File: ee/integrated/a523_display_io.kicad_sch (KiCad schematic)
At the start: 5 parts, among them U201 A523

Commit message: Working on the schematic.
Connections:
- net DSI_CKN renamed DSI.CKN
- net DSI_CKP renamed DSI.CKP
- net DSI_D0N renamed DSI.D0N
- net DSI_D0P renamed DSI.D0P
- net DSI_D1N renamed DSI.D1N
- net DSI_D1P renamed DSI.D1P
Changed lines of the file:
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@@
 		(at 114.3 71.12)
 	)
+	(bus_entry
+		(at 30.48 48.26)
+		(size 2.54 2.54)
+		(stroke
+			(width 0)
+			(type default)
+		)
+	)
+	(bus_entry
+		(at 30.48 45.72)
+		(size 2.54 2.54)
+		(stroke
+			(width 0)
+			(type default)
+		)
+	)
+	(bus_entry
+		(at 30.48 35.56)
+		(size 2.54 2.54)
+		(stroke
+			(width 0)
+			(type default)
+		)
+	)
+	(bus_entry
+		(at 30.48 43.18)
+		(size 2.54 2.54)
+		(stroke
+			(width 0)
+			(type default)
+		)
+	)
+	(bus_entry
+		(at 30.48 38.1)
+		(size 2.54 2.54)
+		(stroke
+			(width 0)
+			(type default)
+		)
+	)
+	(bus_entry
+		(at 30.48 40.64)
+		(size 2.54 2.54)
+		(stroke
+			(width 0)
+			(type default)
+		)
+	)
+	(bus
+		(pts
+			(xy 24.13 29.21) (xy 30.48 29.21)
+		)
+		(stroke
+			(width 0)
+			(type default)
+		)
+	)
 	(wire
 		(pts
@@
 	(wire
 		(pts
-			(xy 53.34 101.6) (xy 48.26 101.6)
+			(xy 43.18 99.06) (xy 43.18 101.6)
 		)
 		(stroke
@@
 	(wire
 		(pts
-			(xy 53.34 43.18) (xy 48.26 43.18)
+			(xy 43.18 101.6) (xy 53.34 101.6)
 		)
 		(stroke
@@
 	(wire
 		(pts
-			(xy 53.34 50.8) (xy 48.26 50.8)
+			(xy 172.72 40.64) (xy 187.96 40.64)
 		)
 		(stroke
@@
 	(wire
 		(pts
-			(xy 53.34 45.72) (xy 48.26 45.72)
+			(xy 48.26 95.25) (xy 48.26 99.06)
 		)
 		(stroke
@@
 	(wire
 		(pts
-			(xy 172.72 40.64) (xy 187.96 40.64)
+			(xy 172.72 48.26) (xy 172.72 50.8)
 		)
 		(stroke
@@
 	(wire
 		(pts
-			(xy 172.72 48.26) (xy 172.72 50.8)
+			(xy 172.72 43.18) (xy 172.72 40.64)
+		)
+		(stroke
+			(width 0)
+			(type default)
+		)
+	)
+	(bus
+		(pts
+			(xy 30.48 29.21) (xy 30.48 48.26)
 		)
 		(stroke
@@
 	(wire
 		(pts
-			(xy 172.72 43.18) (xy 172.72 40.64)
+			(xy 172.72 50.8) (xy 187.96 50.8)
 		)
 		(stroke
@@
 	(wire
 		(pts
-			(xy 172.72 50.8) (xy 187.96 50.8)
+			(xy 53.34 99.06) (xy 48.26 99.06)
 		)
 		(stroke
@@
 	(wire
 		(pts
-			(xy 53.34 99.06) (xy 48.26 99.06)
+			(xy 33.02 43.18) (xy 53.34 43.18)
 		)
 		(stroke
@@
 	(wire
 		(pts
-			(xy 53.34 48.26) (xy 48.26 48.26)
+			(xy 33.02 40.64) (xy 53.34 40.64)
 		)
 		(stroke
@@
 	(wire
 		(pts
-			(xy 53.34 40.64) (xy 48.26 40.64)
+			(xy 33.02 50.8) (xy 53.34 50.8)
 		)
 		(stroke
@@
 	(wire
 		(pts
-			(xy 53.34 38.1) (xy 48.26 38.1)
+			(xy 33.02 45.72) (xy 53.34 45.72)
 		)
 		(stroke
@@
 	(wire
 		(pts
+			(xy 33.02 38.1) (xy 53.34 38.1)
+		)
+		(stroke
+			(width 0)
+			(type default)
+		)
+	)
+	(wire
+		(pts
 			(xy 114.3 78.74) (xy 119.38 78.74)
 		)
@@
 		)
 	)
-	(hierarchical_label "DSI_CKN"
-		(shape bidirectional)
-		(at 48.26 50.8 180)
+	(wire
+		(pts
+			(xy 33.02 48.26) (xy 53.34 48.26)
+		)
+		(stroke
+			(width 0)
+			(type default)
+		)
+	)
+	(label "DSI.D0N"
+		(at 52.07 40.64 180)
 		(effects
 			(font
 				(size 1.27 1.27)
 			)
-			(justify right)
-		)
-	)
-	(hierarchical_label "DSI_CKP"
-		(shape bidirectional)
-		(at 48.26 48.26 180)
+			(justify right bottom)
+		)
+	)
+	(label "DSI.CKN"
+		(at 52.07 50.8 180)
 		(effects
 			(font
 				(size 1.27 1.27)
 			)
-			(justify right)
-		)
-	)
-	(hierarchical_label "DSI_D1P"
-		(shape bidirectional)
-		(at 48.26 43.18 180)
+			(justify right bottom)
+		)
+	)
+	(label "DSI.CKP"
+		(at 52.07 48.26 180)
 		(effects
 			(font
 				(size 1.27 1.27)
 			)
-			(justify right)
-		)
-	)
-	(hierarchical_label "DSI_D1N"
-		(shape bidirectional)
-		(at 48.26 45.72 180)
+			(justify right bottom)
+		)
+	)
+	(label "DSI.D1N"
+		(at 52.07 45.72 180)
 		(effects
 			(font
 				(size 1.27 1.27)
 			)
-			(justify right)
-		)
-	)
-	(hierarchical_label "DSI_D0P"
-		(shape bidirectional)
-		(at 48.26 38.1 180)
+			(justify right bottom)
+		)
+	)
+	(label "DSI.D1P"
+		(at 52.07 43.18 180)
 		(effects
 			(font
 				(size 1.27 1.27)
 			)
-			(justify right)
-		)
-	)
-	(hierarchical_label "DSI_D0N"
-		(shape bidirectional)
-		(at 48.26 40.64 180)
+			(justify right bottom)
+		)
+	)
+	(label "DSI.D0P"
+		(at 52.07 38.1 180)
 		(effects
 			(font
 				(size 1.27 1.27)
 			)
+			(justify right bottom)
+		)
+	)
+	(hierarchical_label "DSI{DSI}"
+		(shape bidirectional)
+		(at 24.13 29.21 180)
+		(effects
+			(font
+				(size 1.27 1.27)
+			)
 			(justify right)
 		)
@@
 	(symbol
 		(lib_id "A523Power:VCC_3V3")
-		(at 48.26 99.06 90)
+		(at 48.26 95.25 0)
 		(unit 1)
 		(body_style 1)
@@
 		(dnp no)
 		(property "Reference" "#PWR0180313568"
-			(at 48.26 99.06 0)
+			(at 48.26 95.25 0)
 			(hide yes)
 			(show_name no)
@@
 		)
 		(property "Value" "VCC_3V3"
-			(at 41.015 99.06 90)
+			(at 48.514 91.694 0)
 			(show_name no)
 			(do_not_autoplace no)
@@
 		)
 		(property "Footprint" ""
-			(at 48.26 99.06 0)
+			(at 48.26 95.25 0)
 			(show_name no)
 			(do_not_autoplace no)
@@
 		)
 		(property "Datasheet" ""
-			(at 48.26 99.06 0)
+			(at 48.26 95.25 0)
 			(show_name no)
 			(do_not_autoplace no)
@@
 		)
 		(property "Description" ""
-			(at 48.26 99.06 0)
+			(at 48.26 95.25 0)
 			(show_name no)
 			(do_not_autoplace no)
@@
 	(symbol
 		(lib_id "A523Power:VCC_1V8")
-		(at 48.26 101.6 90)
+		(at 43.18 99.06 0)
 		(unit 1)
 		(body_style 1)
@@
 		(dnp no)
 		(property "Reference" "#PWR0853362114"
-			(at 48.26 101.6 0)
+			(at 43.18 99.06 0)
 			(hide yes)
 			(show_name no)
@@
 		)
 		(property "Value" "VCC_1V8"
-			(at 41.015 101.6 90)
+			(at 43.18 95.25 0)
 			(show_name no)
 			(do_not_autoplace no)
@@
 		)
 		(property "Footprint" ""
-			(at 48.26 101.6 0)
+			(at 43.18 99.06 0)
 			(show_name no)
 			(do_not_autoplace no)
@@
 		)
 		(property "Datasheet" ""
-			(at 48.26 101.6 0)
+			(at 43.18 99.06 0)
 			(show_name no)
 			(do_not_autoplace no)
@@
 		)
 		(property "Description" ""
-			(at 48.26 101.6 0)
-			(show_name no)
-			(do_not_autoplace no)
+			(at 43.18 99.06 0)
+			(show_name no)
+			(do_not_autoplace no)

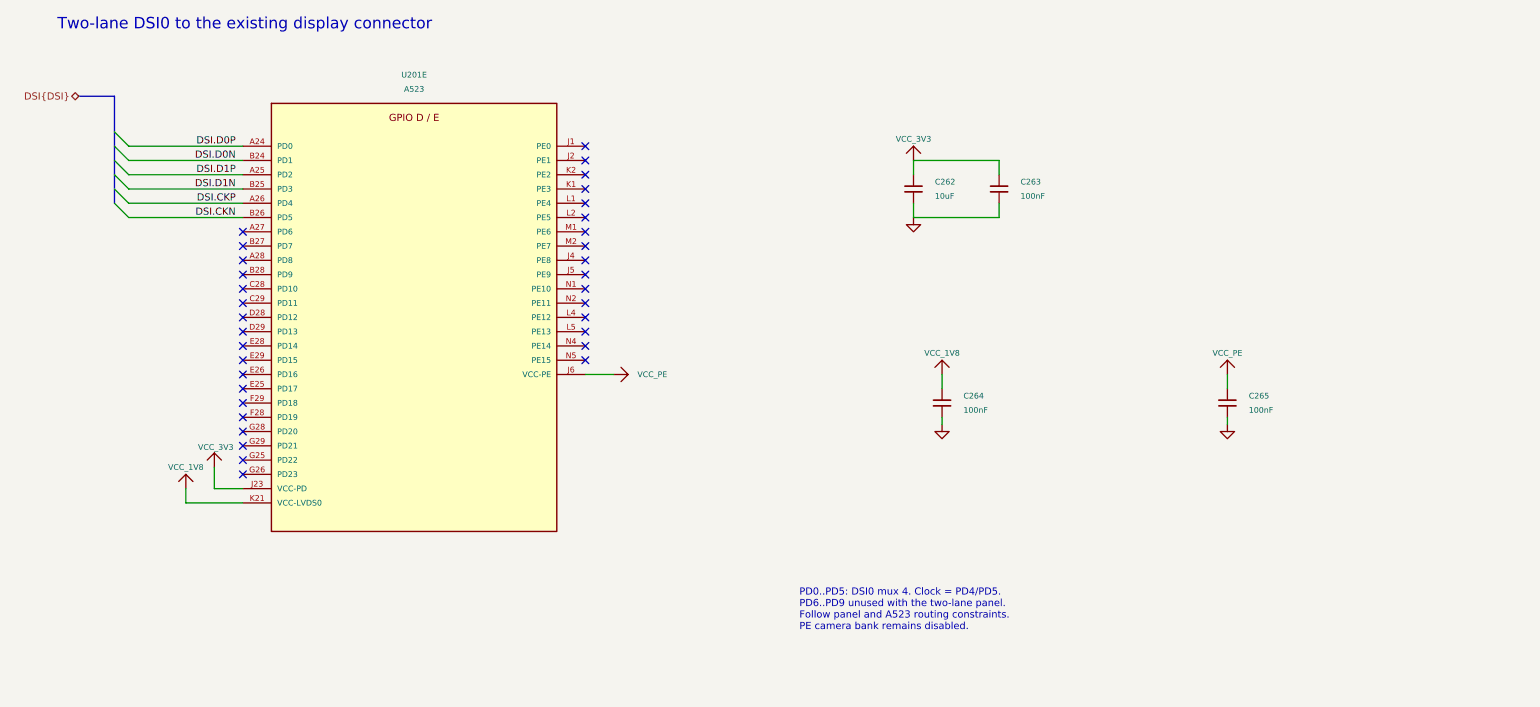
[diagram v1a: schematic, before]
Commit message: Removed USB sheets and moved the parts to the main sheets.
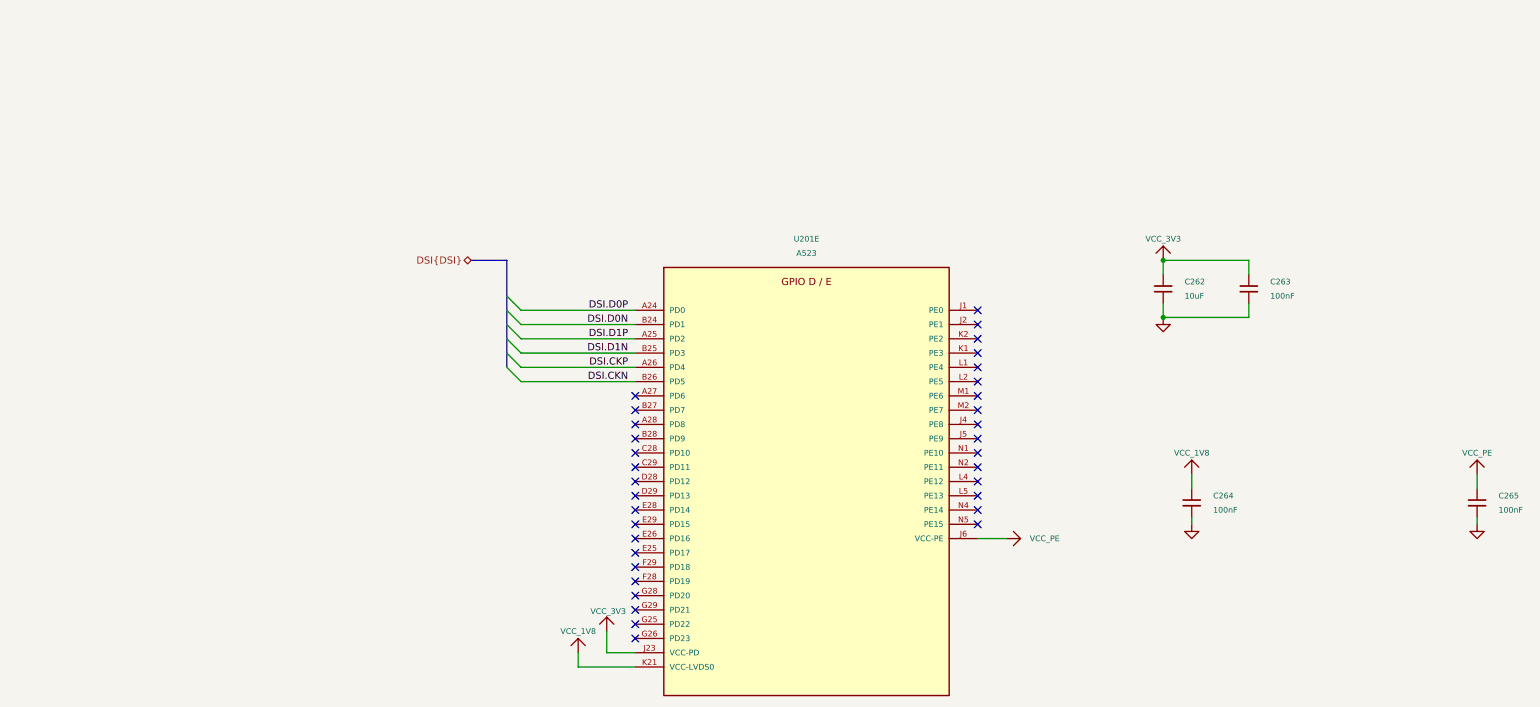
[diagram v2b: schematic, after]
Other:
- note removed: "PD0..PD5: DSI0 mux 4. Clock = PD4/PD5. PD6..PD9 unused with the two-lane panel. Follow panel and A523 routing constraints. PE camera bank remains disabled."
- note removed: "Two-lane DSI0 to the existing display connector"
- moved on the sheet: C262, C263, C264, C265, U201E

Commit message: Worked on the layout.
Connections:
- net VCC_PE renamed +3V3
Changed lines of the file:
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@@
+	(wire
+		(pts
+			(xy 187.96 104.14) (xy 187.96 107.95)
+		)
+		(stroke
+			(width 0)
+			(type default)
+		)
+	)
 	(wire
 		(pts
@@
 	(wire
 		(pts
-			(xy 184.15 107.95) (xy 189.23 107.95)
+			(xy 184.15 107.95) (xy 187.96 107.95)
 		)
 		(stroke
@@
 	)
 	(symbol
+		(lib_id "power:+5V")
+		(at 273.05 96.52 0)
+		(unit 1)
+		(body_style 1)
+		(exclude_from_sim no)
+		(in_bom yes)
+		(on_board yes)
+		(in_pos_files yes)
+		(dnp no)
+		(fields_autoplaced yes)
+		(property "Reference" "#PWR023"
+			(at 273.05 100.33 0)
+			(hide yes)
+			(show_name no)
+			(do_not_autoplace no)
+			(effects
+				(font
+					(size 1.27 1.27)
+				)
+			)
+		)
+		(property "Value" "+3V3"
+			(at 273.05 93.0181 0)
+			(show_name no)
+			(do_not_autoplace no)
+			(effects
+				(font
+					(size 1.27 1.27)
+				)
+			)
+		)
+		(property "Footprint" ""
+			(at 273.05 96.52 0)
+			(hide yes)
+			(show_name no)
+			(do_not_autoplace no)
+			(effects
+				(font
+					(size 1.27 1.27)
+				)
+			)
+		)
+		(property "Datasheet" ""
+			(at 273.05 96.52 0)
+			(hide yes)
+			(show_name no)
+			(do_not_autoplace no)
+			(effects
+				(font
+					(size 1.27 1.27)
+				)
+			)
+		)
+		(property "Description" ""
+			(at 273.05 96.52 0)
+			(show_name no)
+			(do_not_autoplace no)
+			(effects
+				(font
+					(size 1.27 1.27)
+				)
+			)
+		)
+		(pin "1"
+		)
+		(instances
+			(project "blackpants"
+				(path "/d0a98fce-b133-4503-8f8a-83b2a1eed591/9a57dc4c-c52c-4694-b419-f0eeecdbb748"
+					(reference "#PWR023")
+					(unit 1)
+				)
+			)
+		)
+	)
+	(symbol
 		(lib_id "power:GND")
 		(at 273.05 105.41 0)
@@
 				(path "/d0a98fce-b133-4503-8f8a-83b2a1eed591/9a57dc4c-c52c-4694-b419-f0eeecdbb748"
 					(reference "#PWR0250221326")
-					(unit 1)
-				)
-			)
-		)
-	)
-	(symbol
-		(lib_id "A523Power:VCC_PE")
-		(at 189.23 107.95 270)
-		(unit 1)
-		(body_style 1)
-		(exclude_from_sim no)
-		(in_bom no)
-		(on_board yes)
-		(in_pos_files yes)
-		(dnp no)
-		(property "Reference" "#PWR0203783563"
-			(at 189.23 107.95 0)
-			(hide yes)
-			(show_name no)
-			(do_not_autoplace no)
-			(effects
-				(font
-					(size 1.016 1.016)
-				)
-			)
-		)
-		(property "Value" "VCC_PE"
-			(at 196.075 107.95 270)
-			(show_name no)
-			(do_not_autoplace no)
-			(effects
-				(font
-					(size 1.016 1.016)
-				)
-			)
-		)
-		(property "Footprint" ""
-			(at 189.23 107.95 0)
-			(show_name no)
-			(do_not_autoplace no)
-			(effects
-				(font
-					(size 1.27 1.27)
-				)
-			)
-		)
-		(property "Datasheet" ""
-			(at 189.23 107.95 0)
-			(show_name no)
-			(do_not_autoplace no)
-			(effects
-				(font
-					(size 1.27 1.27)
-				)
-			)
-		)
-		(property "Description" ""
-			(at 189.23 107.95 0)
-			(show_name no)
-			(do_not_autoplace no)
-			(effects
-				(font
-					(size 1.27 1.27)
-				)
-			)
-		)
-		(pin "1"
-		)
-		(instances
-			(project "blackpants"
-				(path "/d0a98fce-b133-4503-8f8a-83b2a1eed591/9a57dc4c-c52c-4694-b419-f0eeecdbb748"
-					(reference "#PWR0203783563")
 					(unit 1)
 				)
@@
 	)
 	(symbol
+		(lib_id "power:+5V")
+		(at 187.96 104.14 0)
+		(unit 1)
+		(body_style 1)
+		(exclude_from_sim no)
+		(in_bom yes)
+		(on_board yes)
+		(in_pos_files yes)
+		(dnp no)
+		(fields_autoplaced yes)
+		(property "Reference" "#PWR022"
+			(at 187.96 107.95 0)
+			(hide yes)
+			(show_name no)
+			(do_not_autoplace no)
+			(effects
+				(font
+					(size 1.27 1.27)
+				)
+			)
+		)
+		(property "Value" "+3V3"
+			(at 187.96 100.6381 0)
+			(show_name no)
+			(do_not_autoplace no)
+			(effects
+				(font
+					(size 1.27 1.27)
+				)
+			)
+		)
+		(property "Footprint" ""
+			(at 187.96 104.14 0)
+			(hide yes)
+			(show_name no)
+			(do_not_autoplace no)
+			(effects
+				(font
+					(size 1.27 1.27)
+				)
+			)
+		)
+		(property "Datasheet" ""
+			(at 187.96 104.14 0)
+			(hide yes)
+			(show_name no)
+			(do_not_autoplace no)
+			(effects
+				(font
+					(size 1.27 1.27)
+				)
+			)
+		)
+		(property "Description" ""
+			(at 187.96 104.14 0)
+			(show_name no)
+			(do_not_autoplace no)
+			(effects
+				(font
+					(size 1.27 1.27)
+				)
+			)
+		)
+		(pin "1"
+		)
+		(instances
+			(project "blackpants"
+				(path "/d0a98fce-b133-4503-8f8a-83b2a1eed591/9a57dc4c-c52c-4694-b419-f0eeecdbb748"
+					(reference "#PWR022")
+					(unit 1)
+				)
+			)
+		)
+	)
+	(symbol
 		(lib_id "Device:C_Small")
 		(at 273.05 101.6 0)
@@
 					(unit 1)
 				)
-			)
-		)
-	)
-	(symbol
-		(lib_id "A523Power:VCC_PE")
-		(at 273.05 96.52 0)
-		(unit 1)
-		(body_style 1)
-		(exclude_from_sim no)
-		(in_bom no)
-		(on_board yes)
-		(in_pos_files yes)
-		(dnp no)
-		(property "Reference" "#PWR0651042811"
-			(at 273.05 96.52 0)
-			(hide yes)
-			(show_name no)
-			(do_not_autoplace no)
-			(effects
-				(font
-					(size 1.016 1.016)
-				)
-			)
-		)
-		(property "Value" "VCC_PE"
-			(at 273.05 92.71 0)
-			(show_name no)
-			(do_not_autoplace no)
-			(effects
-				(font
-					(size 1.016 1.016)
-				)
-			)
-		)
-		(property "Footprint" ""
-			(at 273.05 96.52 0)
-			(show_name no)
-			(do_not_autoplace no)
-			(effects
-				(font
-					(size 1.27 1.27)
-				)
-			)
-		)
-		(property "Datasheet" ""
-			(at 273.05 96.52 0)
-			(show_name no)
-			(do_not_autoplace no)
-			(effects
-				(font
-					(size 1.27 1.27)
-				)
-			)
-		)
-		(property "Description" ""
-			(at 273.05 96.52 0)
-			(show_name no)
-			(do_not_autoplace no)
-			(effects
-				(font
-					(size 1.27 1.27)
-				)
-			)
-		)
-		(pin "1"
-		)
-		(instances
-			(project "blackpants"
-				(path "/d0a98fce-b133-4503-8f8a-83b2a1eed591/9a57dc4c-c52c-4694-b419-f0eeecdbb748"
-					(reference "#PWR0651042811")
-					(unit 1)
-				)
